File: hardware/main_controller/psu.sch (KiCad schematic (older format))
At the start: 3 parts

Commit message: Peripherals
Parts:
- added J?: Barrel_Jack, symbol Connector:Barrel_Jack
- added J?: Screw_Terminal_01x02, symbol Connector:Screw_Terminal_01x02
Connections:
- net +5V: now also J?.1, J?.2 (Pin_2)
- net GND: now also J?.1 (Pin_1), J?.2
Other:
- note added: "Power In"
- note added: "Voltage Regulator"
- moved on the sheet: C?, U?
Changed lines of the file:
@@
 $Descr A4 11693 8268
 encoding utf-8
-Sheet 4 6
+Sheet 6 6
 Title ""
 Date ""
@@
 L Regulator_Linear:LM1117-3.3 U?
 U 1 1 5FD3DA15
-P 1500 1100
-F 0 "U?" H 1500 1342 50  0000 C CNN
-F 1 "LM1117-3.3" H 1500 1251 50  0000 C CNN
-F 2 "" H 1500 1100 50  0001 C CNN
-F 3 "http://www.ti.com/lit/ds/symlink/lm1117.pdf" H 1500 1100 50  0001 C CNN
-	1    1500 1100
+P 1250 1150
+F 0 "U?" H 1250 1392 50  0000 C CNN
+F 1 "LM1117-3.3" H 1250 1301 50  0000 C CNN
+F 2 "" H 1250 1150 50  0001 C CNN
+F 3 "http://www.ti.com/lit/ds/symlink/lm1117.pdf" H 1250 1150 50  0001 C CNN
+	1    1250 1150
 	1    0    0    -1
 $EndComp
@@
 L power:+5V #PWR?
 U 1 1 5FD406E4
-P 1050 950
-F 0 "#PWR?" H 1050 800 50  0001 C CNN
-F 1 "+5V" H 1065 1123 50  0000 C CNN
-F 2 "" H 1050 950 50  0001 C CNN
-F 3 "" H 1050 950 50  0001 C CNN
-	1    1050 950
+P 800 1000
+F 0 "#PWR?" H 800 850 50  0001 C CNN
+F 1 "+5V" H 815 1173 50  0000 C CNN
+F 2 "" H 800 1000 50  0001 C CNN
+F 3 "" H 800 1000 50  0001 C CNN
+	1    800  1000
 	1    0    0    -1
 $EndComp
 Wire Wire Line
-	1050 950  1050 1100
+	800  1000 800  1150
 Wire Wire Line
-	1050 1100 1200 1100
+	800  1150 950  1150
 $Comp
 L power:+3V3 #PWR?
 U 1 1 5FD40F8D
-P 1950 950
-F 0 "#PWR?" H 1950 800 50  0001 C CNN
-F 1 "+3V3" H 1965 1123 50  0000 C CNN
-F 2 "" H 1950 950 50  0001 C CNN
-F 3 "" H 1950 950 50  0001 C CNN
-	1    1950 950
+P 1700 1000
+F 0 "#PWR?" H 1700 850 50  0001 C CNN
+F 1 "+3V3" H 1715 1173 50  0000 C CNN
+F 2 "" H 1700 1000 50  0001 C CNN
+F 3 "" H 1700 1000 50  0001 C CNN
+	1    1700 1000
 	1    0    0    -1
 $EndComp
 Wire Wire Line
-	1950 950  1950 1100
+	1700 1000 1700 1150
 Wire Wire Line
-	1950 1100 1800 1100
+	1700 1150 1550 1150
 $Comp
 L power:GND #PWR?
 U 1 1 5FD41E0E
-P 1500 1550
-F 0 "#PWR?" H 1500 1300 50  0001 C CNN
-F 1 "GND" H 1505 1377 50  0000 C CNN
-F 2 "" H 1500 1550 50  0001 C CNN
-F 3 "" H 1500 1550 50  0001 C CNN
-	1    1500 1550
+P 1250 1600
+F 0 "#PWR?" H 1250 1350 50  0001 C CNN
+F 1 "GND" H 1255 1427 50  0000 C CNN
+F 2 "" H 1250 1600 50  0001 C CNN
+F 3 "" H 1250 1600 50  0001 C CNN
+	1    1250 1600
 	1    0    0    -1
 $EndComp
 Wire Wire Line
-	1500 1550 1500 1500
+	1250 1600 1250 1550
 $Comp
 L Device:CP C?
 U 1 1 5FD42713
-P 1050 1350
-F 0 "C?" H 1168 1396 50  0000 L CNN
-F 1 "10uF" H 1168 1305 50  0000 L CNN
-F 2 "" H 1088 1200 50  0001 C CNN
-F 3 "~" H 1050 1350 50  0001 C CNN
-F 4 "Tantalum" H 1050 1350 50  0001 C CNN "Comment"
-	1    1050 1350
+P 800 1400
+F 0 "C?" H 918 1446 50  0000 L CNN
+F 1 "10uF" H 918 1355 50  0000 L CNN
+F 2 "" H 838 1250 50  0001 C CNN
+F 3 "~" H 800 1400 50  0001 C CNN
+F 4 "Tantalum" H 800 1400 50  0001 C CNN "Comment"
+	1    800  1400
 	1    0    0    -1
 $EndComp
@@
 L Device:CP C?
 U 1 1 5FD43191
-P 1950 1350
-F 0 "C?" H 2068 1396 50  0000 L CNN
-F 1 "10uF" H 2068 1305 50  0000 L CNN
-F 2 "" H 1988 1200 50  0001 C CNN
-F 3 "~" H 1950 1350 50  0001 C CNN
-F 4 "Tantalum" H 1950 1350 50  0001 C CNN "Comment"
-	1    1950 1350
+P 1700 1400
+F 0 "C?" H 1818 1446 50  0000 L CNN
+F 1 "10uF" H 1818 1355 50  0000 L CNN
+F 2 "" H 1738 1250 50  0001 C CNN
+F 3 "~" H 1700 1400 50  0001 C CNN
+F 4 "Tantalum" H 1700 1400 50  0001 C CNN "Comment"
+	1    1700 1400
 	1    0    0    -1
 $EndComp
 Wire Wire Line
-	1050 1200 1050 1100
-Connection ~ 1050 1100
+	800  1250 800  1150
+Connection ~ 800  1150
 Wire Wire Line
-	1950 1100 1950 1200
-Connection ~ 1950 1100
+	1700 1150 1700 1250
+Connection ~ 1700 1150
 Wire Wire Line
-	1950 1500 1500 1500
-Connection ~ 1500 1500
+	1700 1550 1250 1550
+Connection ~ 1250 1550
 Wire Wire Line
-	1500 1500 1500 1400
+	1250 1550 1250 1450
 Wire Wire Line
-	1050 1500 1500 1500
+	800  1550 1250 1550
+$Comp
+L Connector:Barrel_Jack J?
+U 1 1 5FE111BC
+P 1350 2500
+F 0 "J?" H 1407 2825 50  0000 C CNN
+F 1 "Barrel_Jack" H 1407 2734 50  0000 C CNN
+F 2 "" H 1400 2460 50  0001 C CNN
+F 3 "~" H 1400 2460 50  0001 C CNN
+	1    1350 2500
+	1    0    0    -1
+$EndComp
+$Comp
+L Connector:Screw_Terminal_01x02 J?
+U 1 1 5FE125BC
+P 1200 3100
+F 0 "J?" H 1118 2775 50  0000 C CNN
+F 1 "Screw_Terminal_01x02" H 1118 2866 50  0000 C CNN
+F 2 "" H 1200 3100 50  0001 C CNN
+F 3 "~" H 1200 3100 50  0001 C CNN
+	1    1200 3100
+	-1   0    0    1
+$EndComp
+$Comp
+L power:+5V #PWR?
+U 1 1 5FE13319
+P 1850 2300
+F 0 "#PWR?" H 1850 2150 50  0001 C CNN
+F 1 "+5V" H 1865 2473 50  0000 C CNN
+F 2 "" H 1850 2300 50  0001 C CNN
+F 3 "" H 1850 2300 50  0001 C CNN
+	1    1850 2300
+	1    0    0    -1
+$EndComp
+Wire Wire Line
+	1850 2300 1850 2400
+Wire Wire Line
+	1850 2400 1650 2400
+Wire Wire Line
+	1400 3000 1850 3000
+Wire Wire Line
+	1850 3000 1850 2400
+Connection ~ 1850 2400
+$Comp
+L power:GND #PWR?
+U 1 1 5FE1482E
+P 1750 3250
+F 0 "#PWR?" H 1750 3000 50  0001 C CNN
+F 1 "GND" H 1755 3077 50  0000 C CNN
+F 2 "" H 1750 3250 50  0001 C CNN
+F 3 "" H 1750 3250 50  0001 C CNN
+	1    1750 3250
+	1    0    0    -1
+$EndComp
+Wire Wire Line
+	1650 2600 1750 2600
+Wire Wire Line
+	1750 2600 1750 3100
+Wire Wire Line
+	1400 3100 1750 3100
+Connection ~ 1750 3100
+Wire Wire Line
+	1750 3100 1750 3250
+Wire Notes Line
+	550  2000 2050 2000
+Wire Notes Line
+	2050 2000 2050 3550
+Wire Notes Line
+	2050 3550 550  3550
+Wire Notes Line
+	550  3550 550  2000
+Text Notes 600  2150 0    89   ~ 0
+Power In
+Wire Notes Line
+	550  550  550  1850
+Wire Notes Line
+	550  1850 2050 1850
+Wire Notes Line
+	550  550  2050 550
+Wire Notes Line
+	2050 550  2050 1850
+Text Notes 600  700  0    89   ~ 0
+Voltage Regulator
 $EndSCHEMATC

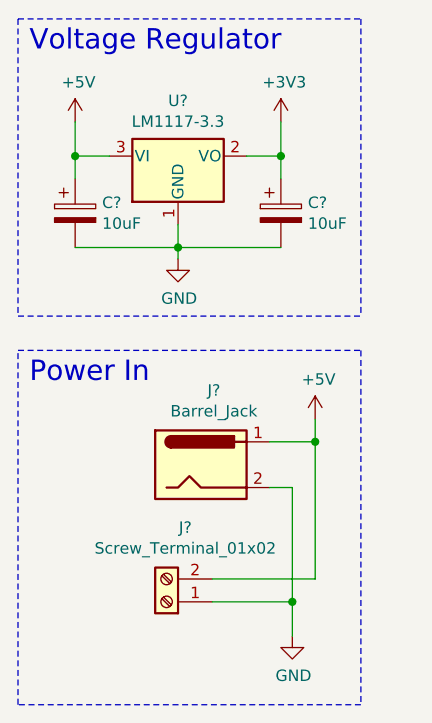
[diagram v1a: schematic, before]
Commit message: Assigned names
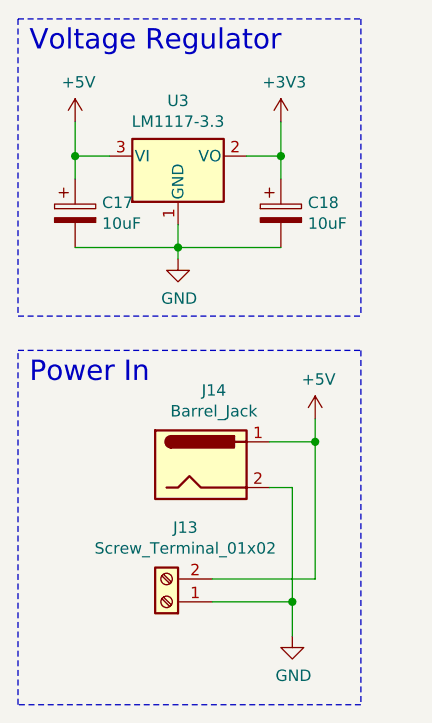
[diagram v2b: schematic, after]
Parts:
- gave numbers to parts that had none: 5
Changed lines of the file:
@@
 $EndDescr
 $Comp
-L Regulator_Linear:LM1117-3.3 U?
+L Regulator_Linear:LM1117-3.3 U3
 U 1 1 5FD3DA15
 P 1250 1150
-F 0 "U?" H 1250 1392 50  0000 C CNN
+F 0 "U3" H 1250 1392 50  0000 C CNN
 F 1 "LM1117-3.3" H 1250 1301 50  0000 C CNN
 F 2 "" H 1250 1150 50  0001 C CNN
@@
 $EndComp
 $Comp
-L power:+5V #PWR?
+L power:+5V #PWR033
 U 1 1 5FD406E4
 P 800 1000
-F 0 "#PWR?" H 800 850 50  0001 C CNN
+F 0 "#PWR033" H 800 850 50  0001 C CNN
 F 1 "+5V" H 815 1173 50  0000 C CNN
 F 2 "" H 800 1000 50  0001 C CNN
@@
 	800  1150 950  1150
 $Comp
-L power:+3V3 #PWR?
+L power:+3V3 #PWR035
 U 1 1 5FD40F8D
 P 1700 1000
-F 0 "#PWR?" H 1700 850 50  0001 C CNN
+F 0 "#PWR035" H 1700 850 50  0001 C CNN
 F 1 "+3V3" H 1715 1173 50  0000 C CNN
 F 2 "" H 1700 1000 50  0001 C CNN
@@
 	1700 1150 1550 1150
 $Comp
-L power:GND #PWR?
+L power:GND #PWR034
 U 1 1 5FD41E0E
 P 1250 1600
-F 0 "#PWR?" H 1250 1350 50  0001 C CNN
+F 0 "#PWR034" H 1250 1350 50  0001 C CNN
 F 1 "GND" H 1255 1427 50  0000 C CNN
 F 2 "" H 1250 1600 50  0001 C CNN
@@
 	1250 1600 1250 1550
 $Comp
-L Device:CP C?
+L Device:CP C17
 U 1 1 5FD42713
 P 800 1400
-F 0 "C?" H 918 1446 50  0000 L CNN
+F 0 "C17" H 918 1446 50  0000 L CNN
 F 1 "10uF" H 918 1355 50  0000 L CNN
 F 2 "" H 838 1250 50  0001 C CNN
@@
 $EndComp
 $Comp
-L Device:CP C?
+L Device:CP C18
 U 1 1 5FD43191
 P 1700 1400
-F 0 "C?" H 1818 1446 50  0000 L CNN
+F 0 "C18" H 1818 1446 50  0000 L CNN
 F 1 "10uF" H 1818 1355 50  0000 L CNN
 F 2 "" H 1738 1250 50  0001 C CNN
@@
 	800  1550 1250 1550
 $Comp
-L Connector:Barrel_Jack J?
+L Connector:Barrel_Jack J14
 U 1 1 5FE111BC
 P 1350 2500
-F 0 "J?" H 1407 2825 50  0000 C CNN
+F 0 "J14" H 1407 2825 50  0000 C CNN
 F 1 "Barrel_Jack" H 1407 2734 50  0000 C CNN
 F 2 "" H 1400 2460 50  0001 C CNN
@@
 $EndComp
 $Comp
-L Connector:Screw_Terminal_01x02 J?
+L Connector:Screw_Terminal_01x02 J13
 U 1 1 5FE125BC
 P 1200 3100
-F 0 "J?" H 1118 2775 50  0000 C CNN
+F 0 "J13" H 1118 2775 50  0000 C CNN
 F 1 "Screw_Terminal_01x02" H 1118 2866 50  0000 C CNN
 F 2 "" H 1200 3100 50  0001 C CNN
@@
 $EndComp
 $Comp
-L power:+5V #PWR?
+L power:+5V #PWR037
 U 1 1 5FE13319
 P 1850 2300
-F 0 "#PWR?" H 1850 2150 50  0001 C CNN
+F 0 "#PWR037" H 1850 2150 50  0001 C CNN
 F 1 "+5V" H 1865 2473 50  0000 C CNN
 F 2 "" H 1850 2300 50  0001 C CNN
@@
 Connection ~ 1850 2400
 $Comp
-L power:GND #PWR?
+L power:GND #PWR036
 U 1 1 5FE1482E
 P 1750 3250
-F 0 "#PWR?" H 1750 3000 50  0001 C CNN
+F 0 "#PWR036" H 1750 3000 50  0001 C CNN
 F 1 "GND" H 1755 3077 50  0000 C CNN
 F 2 "" H 1750 3250 50  0001 C CNN

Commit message: assigned footprints
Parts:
- C17, C18: footprint (none) -> Capacitor_Tantalum_SMD:CP_EIA-3216-10_Kemet-I
- J13: footprint (none) -> TerminalBlock:TerminalBlock_bornier-2_P5.08mm
- J14: footprint (none) -> Connector_BarrelJack:BarrelJack_Wuerth_6941xx301002
- U3: footprint (none) -> Package_TO_SOT_SMD:SOT-223-3_TabPin2
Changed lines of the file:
@@
 F 0 "U3" H 1250 1392 50  0000 C CNN
 F 1 "LM1117-3.3" H 1250 1301 50  0000 C CNN
-F 2 "" H 1250 1150 50  0001 C CNN
+F 2 "Package_TO_SOT_SMD:SOT-223-3_TabPin2" H 1250 1150 50  0001 C CNN
 F 3 "http://www.ti.com/lit/ds/symlink/lm1117.pdf" H 1250 1150 50  0001 C CNN
 	1    1250 1150
@@
 F 0 "C17" H 918 1446 50  0000 L CNN
 F 1 "10uF" H 918 1355 50  0000 L CNN
-F 2 "" H 838 1250 50  0001 C CNN
+F 2 "Capacitor_Tantalum_SMD:CP_EIA-3216-10_Kemet-I" H 838 1250 50  0001 C CNN
 F 3 "~" H 800 1400 50  0001 C CNN
 F 4 "Tantalum" H 800 1400 50  0001 C CNN "Comment"
@@
 F 0 "C18" H 1818 1446 50  0000 L CNN
 F 1 "10uF" H 1818 1355 50  0000 L CNN
-F 2 "" H 1738 1250 50  0001 C CNN
+F 2 "Capacitor_Tantalum_SMD:CP_EIA-3216-10_Kemet-I" H 1738 1250 50  0001 C CNN
 F 3 "~" H 1700 1400 50  0001 C CNN
 F 4 "Tantalum" H 1700 1400 50  0001 C CNN "Comment"
@@
 F 0 "J14" H 1407 2825 50  0000 C CNN
 F 1 "Barrel_Jack" H 1407 2734 50  0000 C CNN
-F 2 "" H 1400 2460 50  0001 C CNN
+F 2 "Connector_BarrelJack:BarrelJack_Wuerth_6941xx301002" H 1400 2460 50  0001 C CNN
 F 3 "~" H 1400 2460 50  0001 C CNN
 	1    1350 2500
@@
 F 0 "J13" H 1118 2775 50  0000 C CNN
 F 1 "Screw_Terminal_01x02" H 1118 2866 50  0000 C CNN
-F 2 "" H 1200 3100 50  0001 C CNN
+F 2 "TerminalBlock:TerminalBlock_bornier-2_P5.08mm" H 1200 3100 50  0001 C CNN
 F 3 "~" H 1200 3100 50  0001 C CNN
 	1    1200 3100

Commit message: pcb
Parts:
- removed J13: Screw_Terminal_01x02, TerminalBlock:TerminalBlock_bornier-2_P5.08mm, symbol Connector:Screw_Terminal_01x02
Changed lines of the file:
@@
-$EndComp
-$Comp
-L Connector:Screw_Terminal_01x02 J13
-U 1 1 5FE125BC
-P 1200 3100
-F 0 "J13" H 1118 2775 50  0000 C CNN
-F 1 "Screw_Terminal_01x02" H 1118 2866 50  0000 C CNN
-F 2 "TerminalBlock:TerminalBlock_bornier-2_P5.08mm" H 1200 3100 50  0001 C CNN
-F 3 "~" H 1200 3100 50  0001 C CNN
-	1    1200 3100
-	-1   0    0    1
 $EndComp
 $Comp
@@
 Wire Wire Line
 	1850 2400 1650 2400
-Wire Wire Line
-	1400 3000 1850 3000
-Wire Wire Line
-	1850 3000 1850 2400
-Connection ~ 1850 2400
 $Comp
 L power:GND #PWR036
 U 1 1 5FE1482E
-P 1750 3250
-F 0 "#PWR036" H 1750 3000 50  0001 C CNN
-F 1 "GND" H 1755 3077 50  0000 C CNN
-F 2 "" H 1750 3250 50  0001 C CNN
-F 3 "" H 1750 3250 50  0001 C CNN
-	1    1750 3250
+P 1850 2750
+F 0 "#PWR036" H 1850 2500 50  0001 C CNN
+F 1 "GND" H 1855 2577 50  0000 C CNN
+F 2 "" H 1850 2750 50  0001 C CNN
+F 3 "" H 1850 2750 50  0001 C CNN
+	1    1850 2750
 	1    0    0    -1
 $EndComp
-Wire Wire Line
-	1650 2600 1750 2600
-Wire Wire Line
-	1750 2600 1750 3100
-Wire Wire Line
-	1400 3100 1750 3100
-Connection ~ 1750 3100
-Wire Wire Line
-	1750 3100 1750 3250
 Wire Notes Line
 	550  2000 2050 2000
@@
 Text Notes 600  700  0    89   ~ 0
 Voltage Regulator
+Wire Wire Line
+	1850 2600 1850 2750
+Wire Wire Line
+	1650 2600 1850 2600
 $EndSCHEMATC
